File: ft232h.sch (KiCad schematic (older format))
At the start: 14 parts, among them U3 93LCxxB, U4 FT232H, Y1 Crystal_GND24

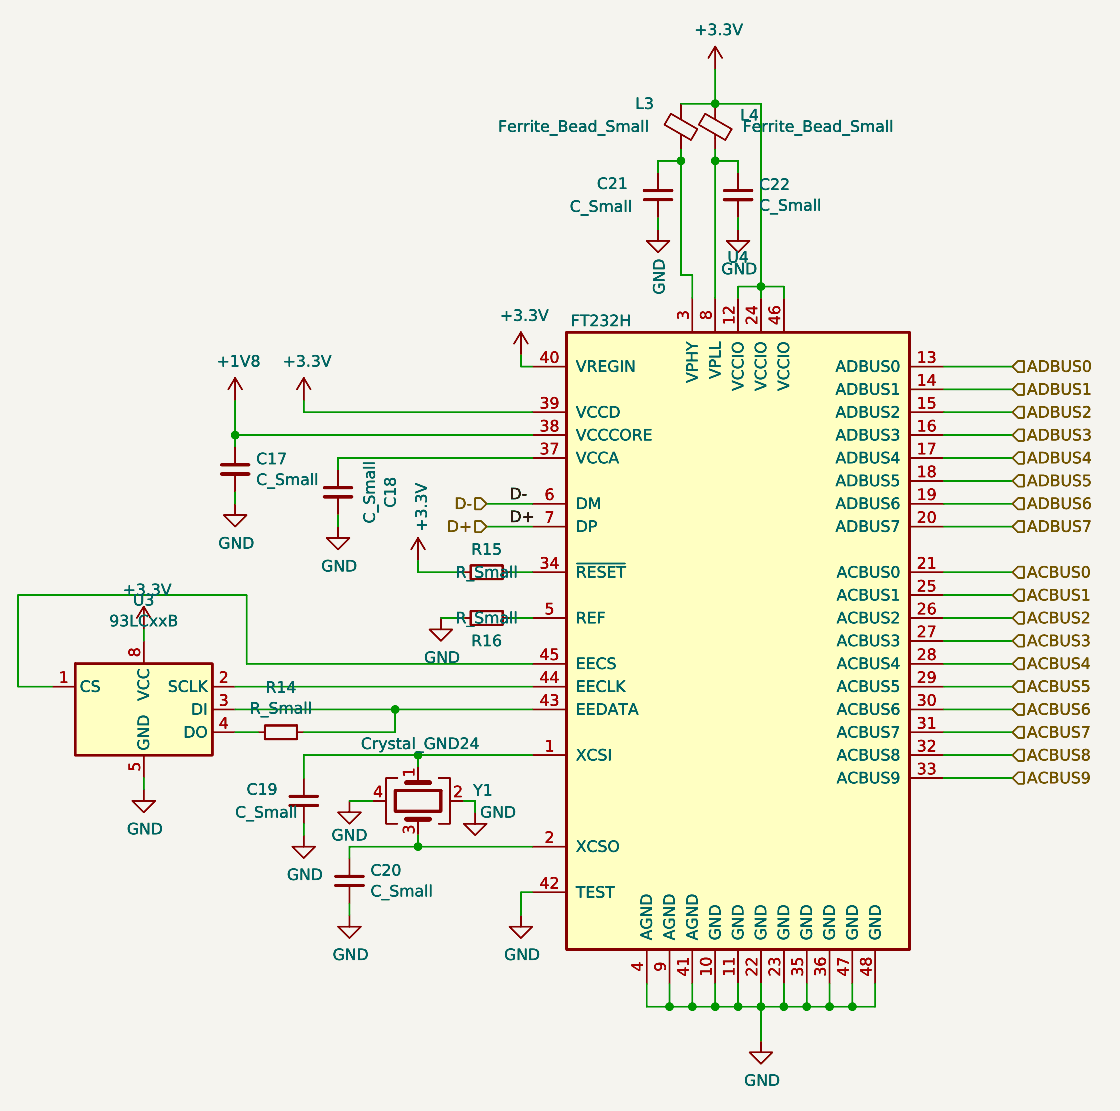
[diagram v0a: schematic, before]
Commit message: revised ethernet layout
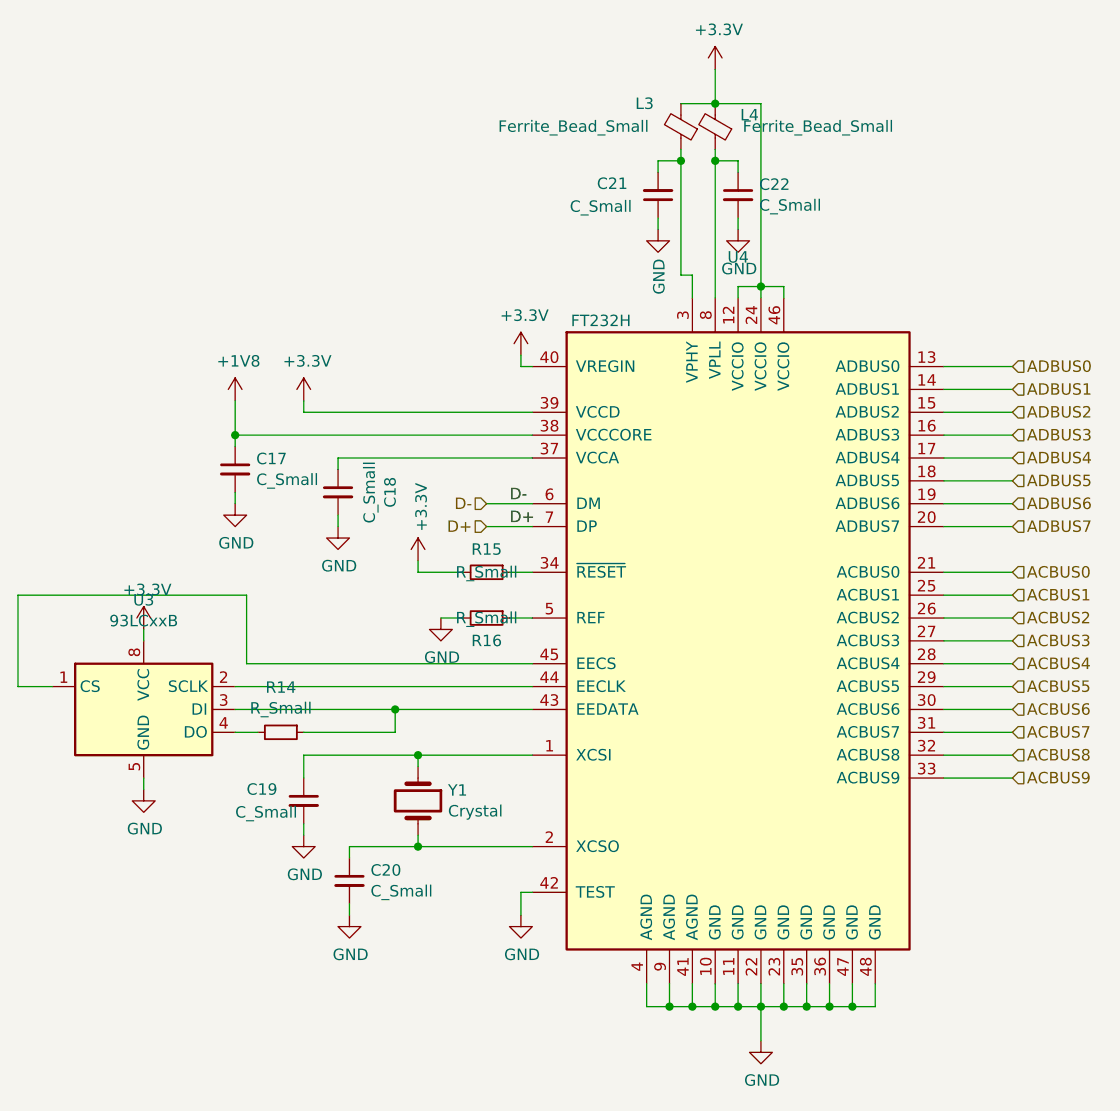
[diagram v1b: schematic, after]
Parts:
- removed Y1: Crystal_GND24, Crystals:Crystal_SMD_3225-4pin_3.2x2.5mm, symbol Device:Crystal_GND24
- added Y1: Crystal, Crystal:Crystal_HC49-U_Vertical, symbol Device:Crystal
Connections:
- net at C19.1, U4.1 (XCSI): now also Y1.1
- net at C20.1, U4.2 (XCSO): now also Y1.2
